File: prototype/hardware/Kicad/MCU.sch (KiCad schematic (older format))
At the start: 17 parts

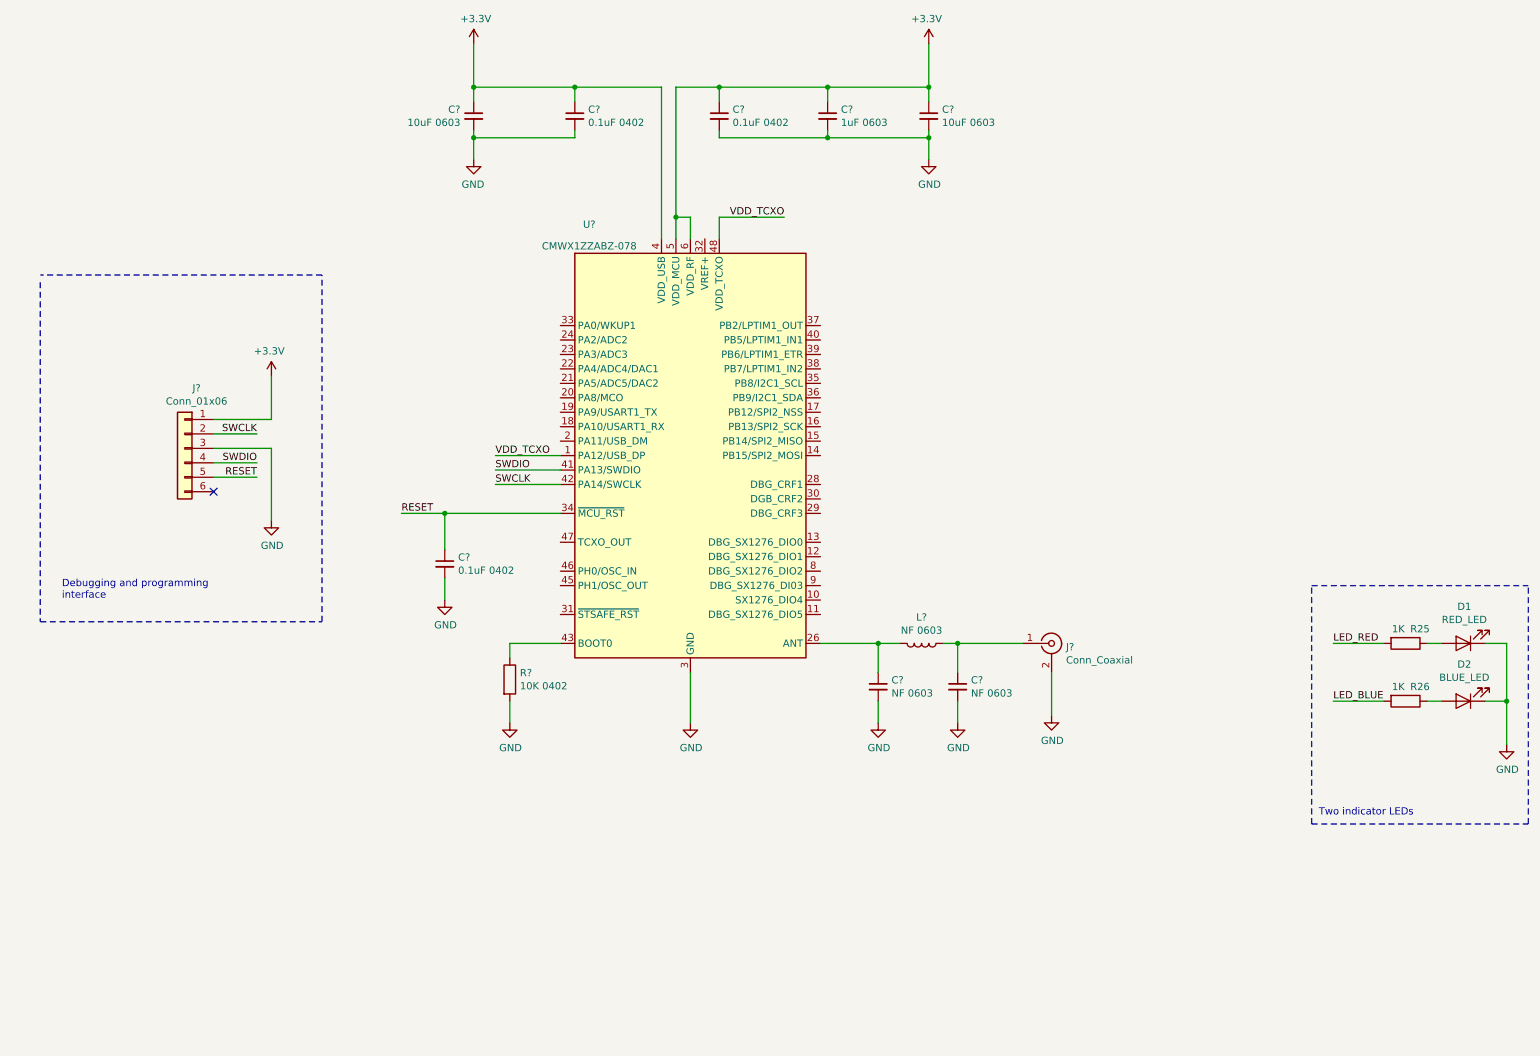
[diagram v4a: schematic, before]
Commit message: Moved all schematic parts  to a single sheet
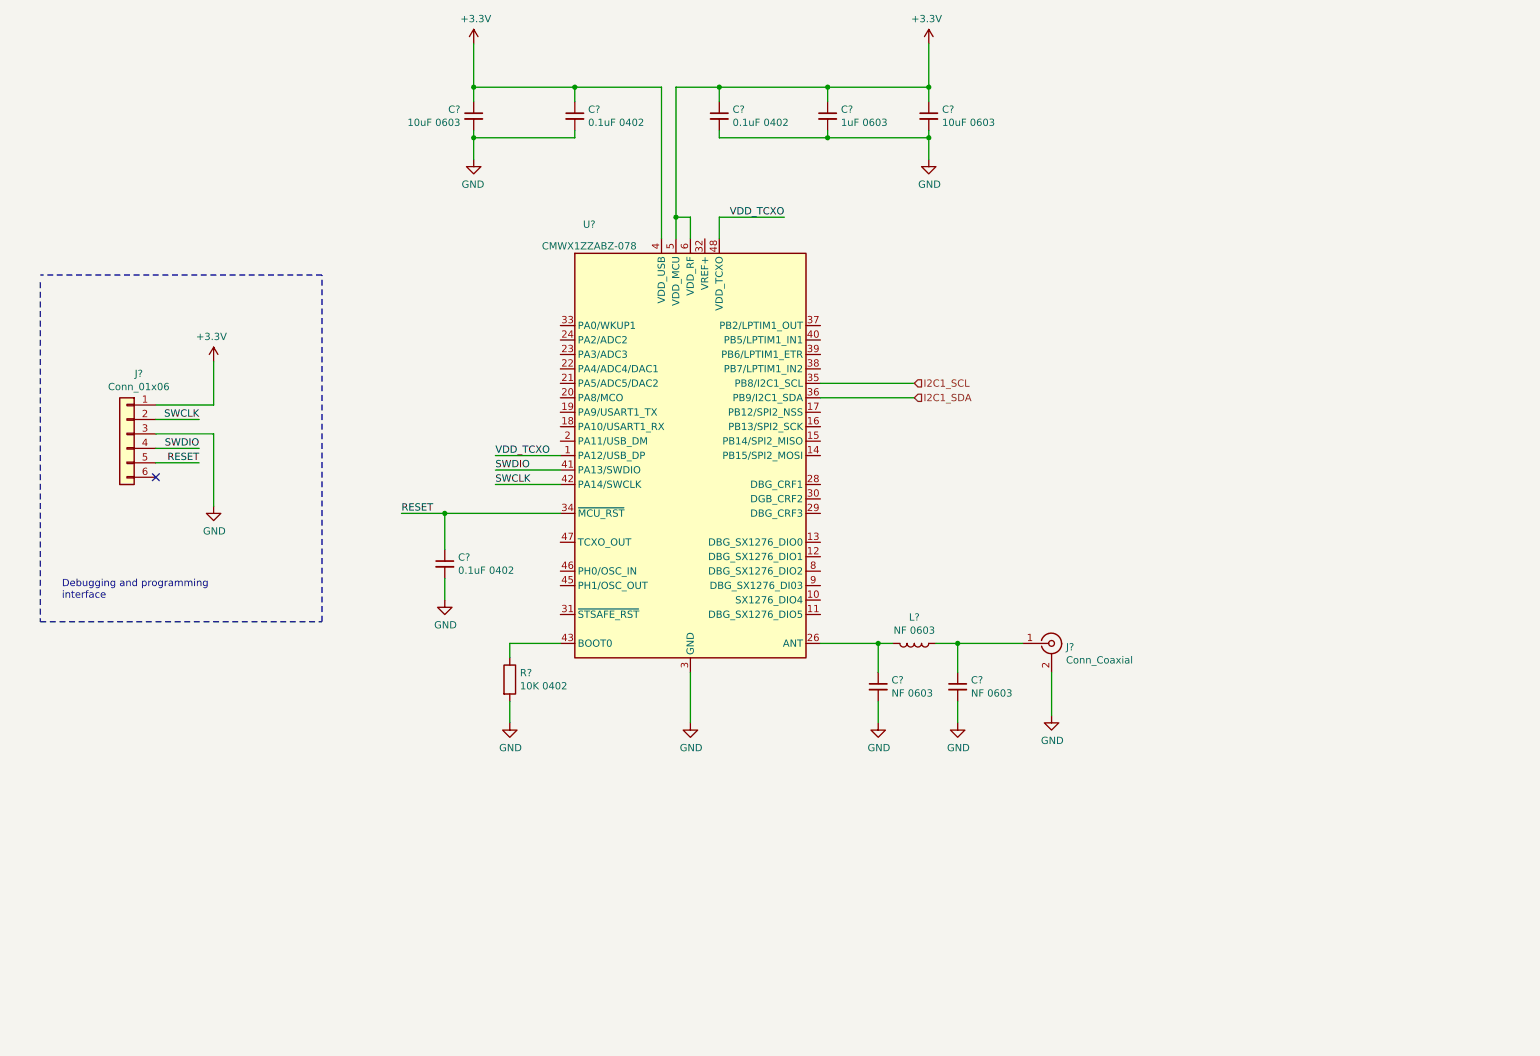
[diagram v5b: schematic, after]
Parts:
- removed D1: RED_LED, LED_SMD:LED_0603_1608Metric, symbol Device:LED
- removed D2: BLUE_LED, LED_SMD:LED_0603_1608Metric, symbol Device:LED
- removed R25, R26: 1K, Resistor_SMD:R_0603_1608Metric, symbol Device:R
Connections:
- net I2C1_SCL: now reaches U?.35 (PB8/I2C1_SCL)
- net I2C1_SDA: now reaches U?.36 (PB9/I2C1_SDA)
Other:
- note removed: "Two indicator LEDs"
- moved on the sheet: J?, L?
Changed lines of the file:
@@
 $Descr A4 11693 8268
 encoding utf-8
-Sheet 5 5
-Title ""
-Date "2019-09-09"
+Sheet 4 5
+Title "Pico lora tracker"
+Date "2019-10-19"
 Rev "1.0"
 Comp "Imperial College Space Society"
-Comment1 ""
+Comment1 "Based on the Picotracker MK II and Project mach one flight computer"
 Comment2 ""
 Comment3 ""
 Comment4 ""
 $EndDescr
-$Comp
-L power:GND #PWR0106
-U 1 1 5D8CC1E1
-P 10900 5600
-F 0 "#PWR0106" H 10900 5350 50  0001 C CNN
-F 1 "GND" H 10905 5427 50  0000 C CNN
-F 2 "" H 10900 5600 50  0001 C CNN
-F 3 "" H 10900 5600 50  0001 C CNN
-	1    10900 5600
-	1    0    0    -1
-$EndComp
-Wire Wire Line
-	10900 5300 10900 5600
-Connection ~ 10900 5300
-Wire Wire Line
-	10900 4900 10900 5300
-Wire Wire Line
-	10050 4900 9700 4900
-Wire Wire Line
-	10050 5300 9700 5300
-Text Label 9700 5300 0    50   ~ 0
-LED_BLUE
-Text Label 9700 4900 0    50   ~ 0
-LED_RED
-Wire Wire Line
-	10350 5300 10450 5300
-Wire Wire Line
-	10750 5300 10900 5300
-Wire Wire Line
-	10350 4900 10450 4900
-Wire Wire Line
-	10750 4900 10900 4900
-Wire Notes Line
-	9550 6150 11050 6150
-Text Notes 9600 6100 0    50   ~ 0
-Two indicator LEDs
-$Comp
-L Device:R R25
-U 1 1 5D84A9D3
-P 10200 4900
-F 0 "R25" V 10100 5000 50  0000 C CNN
-F 1 "1K" V 10100 4850 50  0000 C CNN
-F 2 "Resistor_SMD:R_0603_1608Metric" V 10130 4900 50  0001 C CNN
-F 3 "~" H 10200 4900 50  0001 C CNN
-F 4 "0.035" H 10200 4900 50  0001 C CNN "Cost"
-F 5 "https://uk.rs-online.com/web/p/surface-mount-fixed-resistors/2132266/" H 10200 4900 50  0001 C CNN "Purchase link"
-F 6 "50" H 10200 4900 50  0001 C CNN "min_quantity"
-	1    10200 4900
-	0    1    1    0
-$EndComp
-$Comp
-L Device:LED D1
-U 1 1 5D84CD91
-P 10600 4900
-F 0 "D1" H 10593 4645 50  0000 C CNN
-F 1 "RED_LED" H 10593 4736 50  0000 C CNN
-F 2 "LED_SMD:LED_0603_1608Metric" H 10600 4900 50  0001 C CNN
-F 3 "~" H 10600 4900 50  0001 C CNN
-F 4 "0.038" H 10600 4900 50  0001 C CNN "Cost"
-F 5 "https://uk.rs-online.com/web/p/leds/0450711/" H 10600 4900 50  0001 C CNN "Purchase link"
-F 6 "50" H 10600 4900 50  0001 C CNN "min_quantity"
-	1    10600 4900
-	-1   0    0    1
-$EndComp
-$Comp
-L Device:R R26
-U 1 1 5D8A257E
-P 10200 5300
-F 0 "R26" V 10100 5400 50  0000 C CNN
-F 1 "1K" V 10100 5250 50  0000 C CNN
-F 2 "Resistor_SMD:R_0603_1608Metric" V 10130 5300 50  0001 C CNN
-F 3 "~" H 10200 5300 50  0001 C CNN
-F 4 "0.035" H 10200 5300 50  0001 C CNN "Cost"
-F 5 "https://uk.rs-online.com/web/p/surface-mount-fixed-resistors/2132266/" H 10200 5300 50  0001 C CNN "Purchase link"
-F 6 "50" H 10200 5300 50  0001 C CNN "min_quantity"
-	1    10200 5300
-	0    1    1    0
-$EndComp
-$Comp
-L Device:LED D2
-U 1 1 5D8A258A
-P 10600 5300
-F 0 "D2" H 10593 5045 50  0000 C CNN
-F 1 "BLUE_LED" H 10593 5136 50  0000 C CNN
-F 2 "LED_SMD:LED_0603_1608Metric" H 10600 5300 50  0001 C CNN
-F 3 "~" H 10600 5300 50  0001 C CNN
-	1    10600 5300
-	-1   0    0    1
-$EndComp
-Wire Notes Line
-	9550 4500 11050 4500
-Wire Notes Line
-	11050 6150 11050 4500
-Wire Notes Line
-	9550 6150 9550 4500
 $Comp
 L RF_Module:CMWX1ZZABZ-078 U?
@@
 	4000 5300 4000 5450
 Wire Wire Line
-	1950 3350 2350 3350
-Wire Wire Line
-	2350 3350 2350 3050
+	1550 3250 1950 3250
+Wire Wire Line
+	1950 3250 1950 2950
 $Comp
 L power:+3.3V #PWR?
 U 1 1 5DB55728
-P 2350 3050
-F 0 "#PWR?" H 2350 2900 50  0001 C CNN
-F 1 "+3.3V" H 2365 3223 50  0000 C CNN
-F 2 "" H 2350 3050 50  0001 C CNN
-F 3 "" H 2350 3050 50  0001 C CNN
-	1    2350 3050
+P 1950 2950
+F 0 "#PWR?" H 1950 2800 50  0001 C CNN
+F 1 "+3.3V" H 1965 3123 50  0000 C CNN
+F 2 "" H 1950 2950 50  0001 C CNN
+F 3 "" H 1950 2950 50  0001 C CNN
+	1    1950 2950
 	-1   0    0    -1
 $EndComp
@@
 L Connector_Generic:Conn_01x06 J?
 U 1 1 5DB45FE9
-P 1750 3550
-F 0 "J?" H 1668 3967 50  0000 C CNN
-F 1 "Conn_01x06" H 1668 3876 50  0000 C CNN
-F 2 "" H 1750 3550 50  0001 C CNN
-F 3 "~" H 1750 3550 50  0001 C CNN
-	1    1750 3550
+P 1350 3450
+F 0 "J?" H 1268 3867 50  0000 C CNN
+F 1 "Conn_01x06" H 1268 3776 50  0000 C CNN
+F 2 "" H 1350 3450 50  0001 C CNN
+F 3 "~" H 1350 3450 50  0001 C CNN
+	1    1350 3450
 	-1   0    0    -1
 $EndComp
@@
 SWDIO
 Wire Wire Line
-	1950 3450 2250 3450
-Wire Wire Line
-	1950 3550 2350 3550
-Wire Wire Line
-	2350 3550 2350 4050
-Wire Wire Line
-	1950 3650 2250 3650
-NoConn ~ 1950 3850
+	1550 3350 1850 3350
+Wire Wire Line
+	1550 3450 1950 3450
+Wire Wire Line
+	1950 3450 1950 3950
+Wire Wire Line
+	1550 3550 1850 3550
+NoConn ~ 1550 3750
 Text Label 3900 3800 0    50   ~ 0
 SWCLK
 Wire Wire Line
 	3900 3800 4350 3800
-Text Label 2250 3450 2    50   ~ 0
+Text Label 1850 3350 2    50   ~ 0
 SWCLK
-Text Label 2250 3650 2    50   ~ 0
+Text Label 1850 3550 2    50   ~ 0
 SWDIO
 $Comp
 L power:GND #PWR?
 U 1 1 5DB70B69
-P 2350 4050
-F 0 "#PWR?" H 2350 3800 50  0001 C CNN
-F 1 "GND" H 2355 3877 50  0000 C CNN
-F 2 "" H 2350 4050 50  0001 C CNN
-F 3 "" H 2350 4050 50  0001 C CNN
-	1    2350 4050
+P 1950 3950
+F 0 "#PWR?" H 1950 3700 50  0001 C CNN
+F 1 "GND" H 1955 3777 50  0000 C CNN
+F 2 "" H 1950 3950 50  0001 C CNN
+F 3 "" H 1950 3950 50  0001 C CNN
+	1    1950 3950
 	1    0    0    -1
 $EndComp
@@
 Debugging and programming\ninterface
 Wire Wire Line
-	1950 3750 2250 3750
-Text Label 2250 3750 2    50   ~ 0
+	1550 3650 1850 3650
+Text Label 1850 3650 2    50   ~ 0
 RESET
 Wire Wire Line
@@
 Connection ~ 6550 4900
 Wire Wire Line
-	6550 4900 6700 4900
+	6550 4900 6650 4900
 $Comp
 L power:GND #PWR?
@@
 L Device:L L?
 U 1 1 5DBD576A
-P 6850 4900
-F 0 "L?" V 6669 4900 50  0000 C CNN
-F 1 "NF 0603" V 6760 4900 50  0000 C CNN
-F 2 "" H 6850 4900 50  0001 C CNN
-F 3 "~" H 6850 4900 50  0001 C CNN
-	1    6850 4900
+P 6800 4900
+F 0 "L?" V 6619 4900 50  0000 C CNN
+F 1 "NF 0603" V 6710 4900 50  0000 C CNN
+F 2 "" H 6800 4900 50  0001 C CNN
+F 3 "~" H 6800 4900 50  0001 C CNN
+	1    6800 4900
 	0    1    1    0
 $EndComp
 Wire Wire Line
-	7000 4900 7100 4900
+	6950 4900 7100 4900
+Wire Wire Line
+	6150 3100 6800 3100
+Wire Wire Line
+	6150 3200 6800 3200
+Text HLabel 6800 3100 2    50   Input ~ 0
+I2C1_SCL
+Text HLabel 6800 3200 2    50   Input ~ 0
+I2C1_SDA
 $EndSCHEMATC
